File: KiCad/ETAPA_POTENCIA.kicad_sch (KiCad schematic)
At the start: 9 parts, among them U1 LM1117DT-3.3

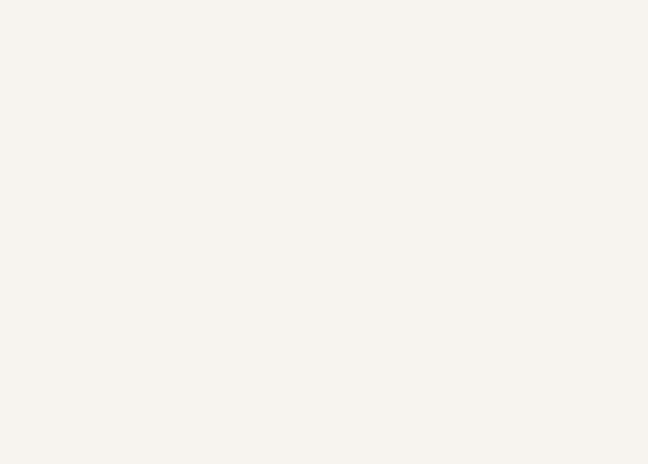
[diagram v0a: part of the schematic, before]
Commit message: Esquematic BUS creat + Diagrama blocs v.3.
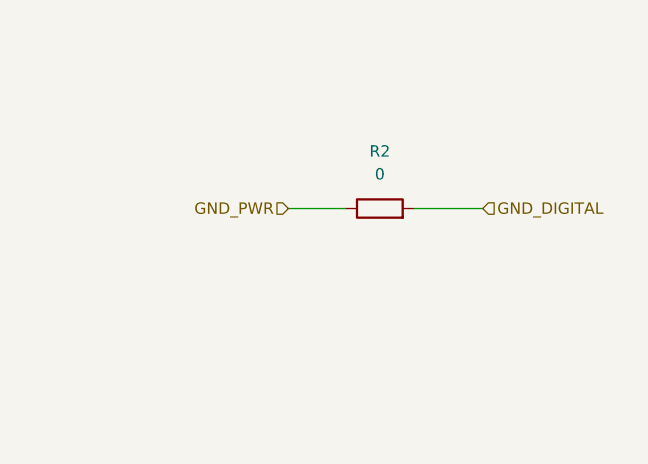
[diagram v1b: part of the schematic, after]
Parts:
- added R2: 0, symbol Device:R
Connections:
- net GND_PWR: now also R2.1
- new net GND_DIGITAL: R2.2
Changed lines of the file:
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@@
+	(wire
+		(pts
+			(xy 210.82 35.56) (xy 217.17 35.56)
+		)
+		(stroke
+			(width 0)
+			(type default)
+		)
+	)
 	(wire
 		(pts
@@
 	(wire
 		(pts
+			(xy 224.79 35.56) (xy 232.41 35.56)
+		)
+		(stroke
+			(width 0)
+			(type default)
+		)
+	)
+	(wire
+		(pts
 			(xy 104.14 34.29) (xy 104.14 36.83)
 		)
@@
 			(width 0)
 			(type default)
+		)
+	)
+	(hierarchical_label "GND_DIGITAL"
+		(shape input)
+		(at 232.41 35.56 0)
+		(effects
+			(font
+				(size 1.27 1.27)
+			)
+			(justify left)
 		)
 	)
@@
 			)
 			(justify left)
+		)
+	)
+	(hierarchical_label "GND_PWR"
+		(shape input)
+		(at 210.82 35.56 180)
+		(effects
+			(font
+				(size 1.27 1.27)
+			)
+			(justify right)
 		)
 	)
@@
 					(unit 1)
 				)
+			)
+		)
+	)
+	(symbol
+		(lib_id "Device:R")
+		(at 220.98 35.56 90)
+		(unit 1)
+		(exclude_from_sim no)
+		(in_bom yes)
+		(on_board yes)
+		(dnp no)
+		(fields_autoplaced yes)
+		(property "Reference" "R2"
+			(at 220.98 29.21 90)
+			(effects
+				(font
+					(size 1.27 1.27)
+				)
+			)
+		)
+		(property "Value" "0"
+			(at 220.98 31.75 90)
+			(effects
+				(font
+					(size 1.27 1.27)
+				)
+			)
+		)
+		(property "Footprint" ""
+			(at 220.98 37.338 90)
+			(effects
+				(font
+					(size 1.27 1.27)
+				)
+				(hide yes)
+			)
+		)
+		(property "Datasheet" "~"
+			(at 220.98 35.56 0)
+			(effects
+				(font
+					(size 1.27 1.27)
+				)
+				(hide yes)
+			)
+		)
+		(property "Description" "Resistor"
+			(at 220.98 35.56 0)
+			(effects
+				(font
+					(size 1.27 1.27)
+				)
+				(hide yes)
+			)
+		)
+		(pin "2"
+		)
+		(pin "1"
+		)
+		(instances
+			(project ""
+				(path "/347831db-5db9-4aff-ad32-e56fd770e219/a8709361-50f1-45a9-9990-4a11f8b46576"
+					(reference "R2")
+					(unit 1)
+				)
